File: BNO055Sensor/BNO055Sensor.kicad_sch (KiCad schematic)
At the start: 3 parts, among them J1 addon_conn

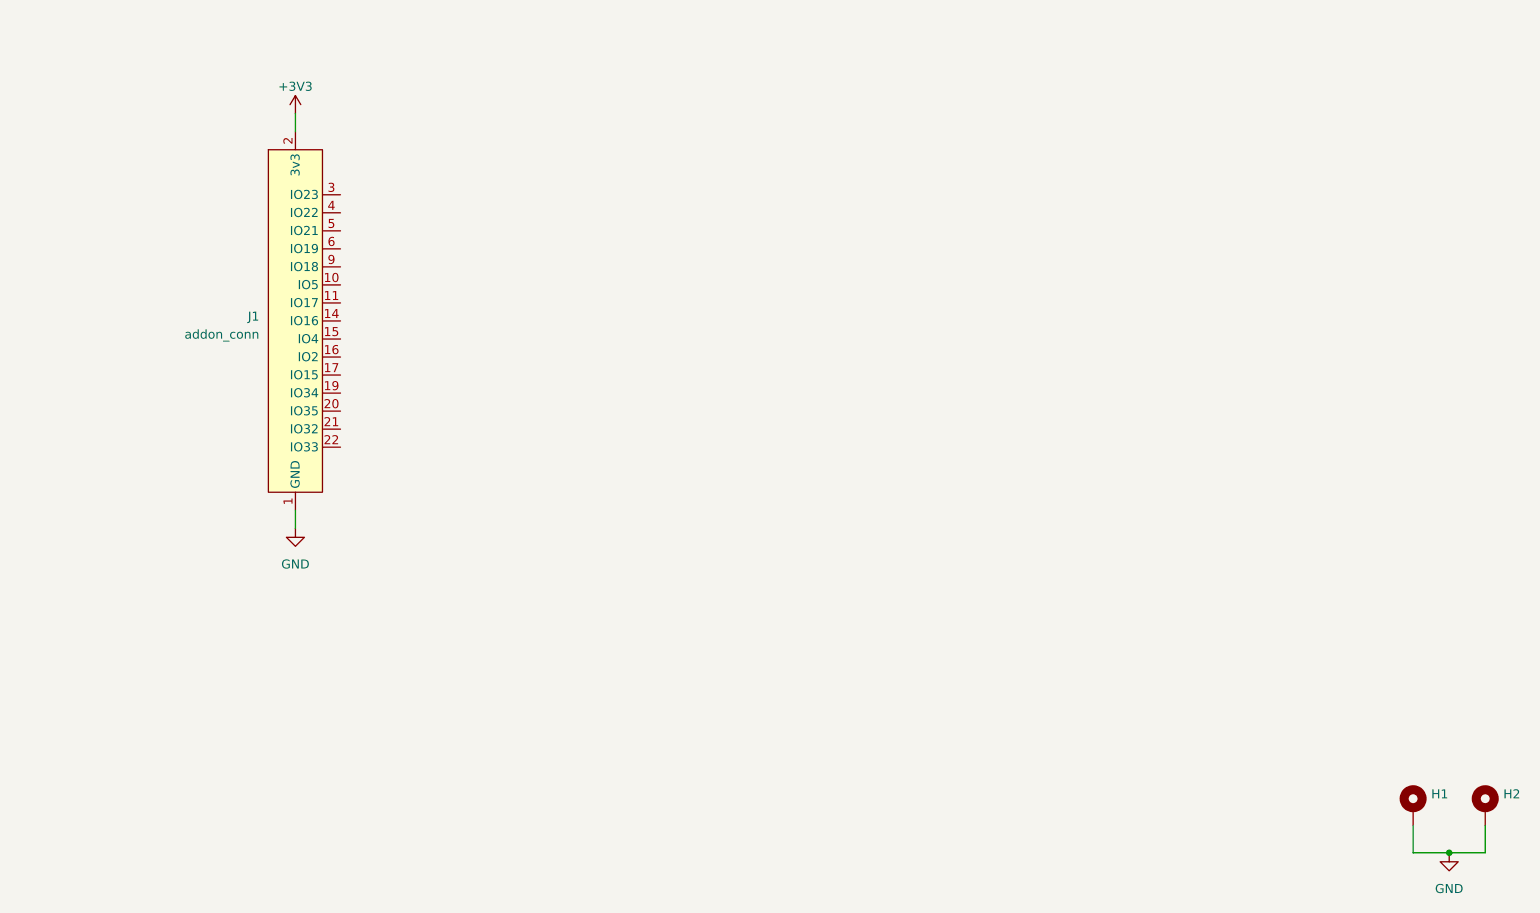
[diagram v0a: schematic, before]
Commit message: Adds BNO055 sensor to schematics
The unused pins are disconnected for now. If we have pins left after
adding other components, we can connect them.

3v3 is connected to the board through a jumper that's normally closed to
Vin since that should be the pin used. In the prototype, 3vo was used
and worked. After we confirm the PCB works with 3v3 connected to Vin as
expected, we can remove this jumper.
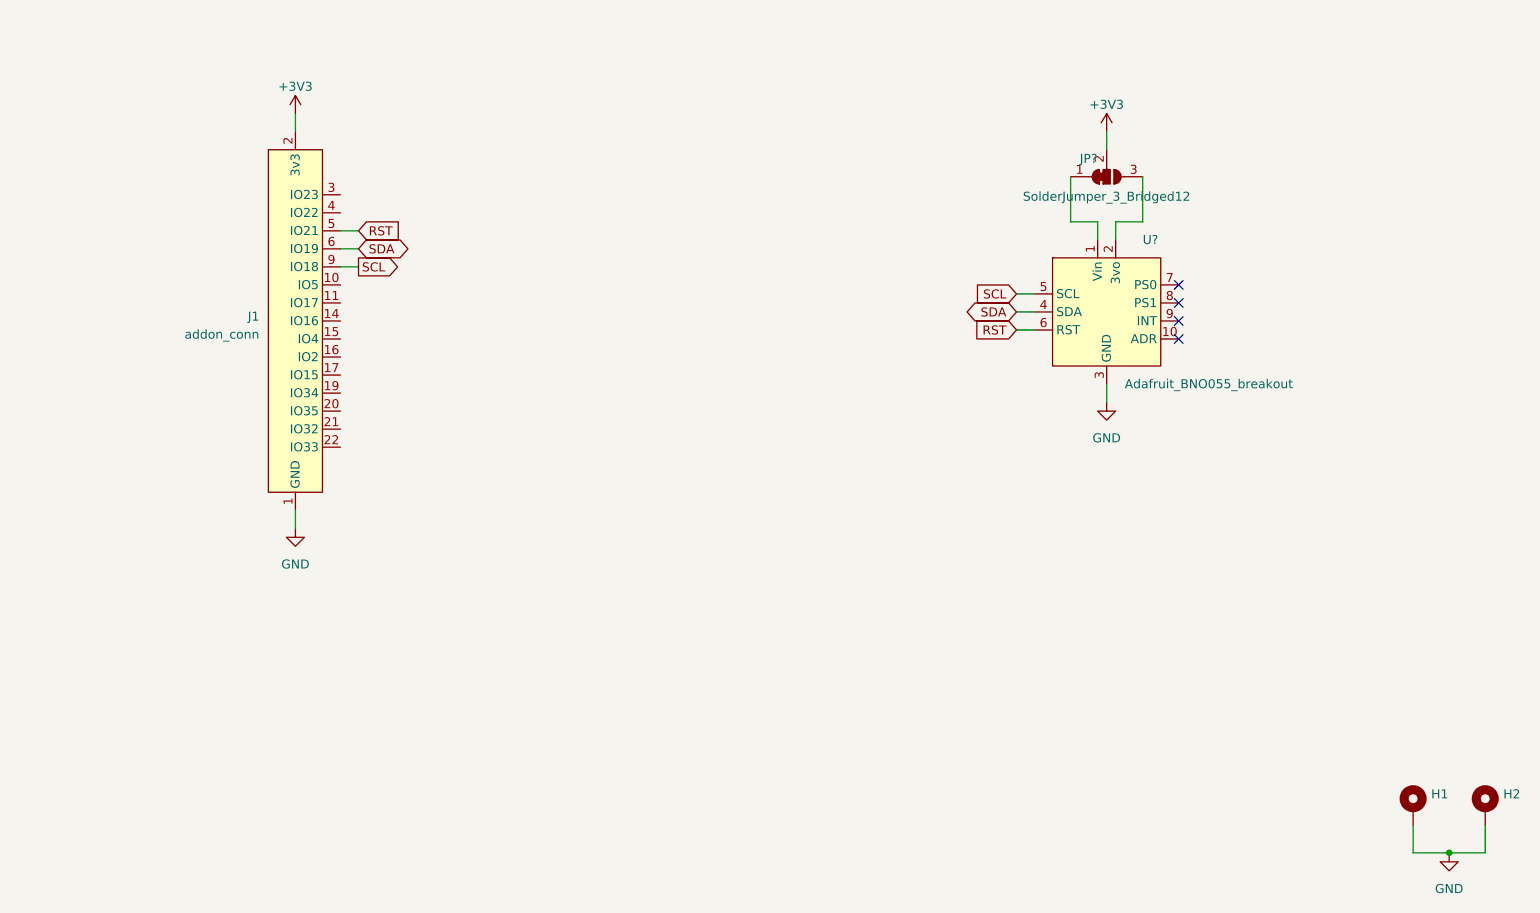
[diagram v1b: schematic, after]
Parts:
- added JP?: SolderJumper_3_Bridged12, symbol Jumper:SolderJumper_3_Bridged12
- added U?: Adafruit_BNO055_breakout, GameOver:Adafruit_BNO055_breakout, symbol GameOver:Adafruit_BNO055_breakout
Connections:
- net +3V3: now also JP?.2 (C)
- net GND: now also U?.3 (GND)
- net RST: now reaches J1.5 (IO21)
- net RST: now also U?.6 (RST)
- net SDA: now reaches J1.6 (IO19)
- net SDA: now also U?.4 (SDA)
- net SCL: now reaches J1.9 (IO18)
- net SCL: now also U?.5 (SCL)
- new net: JP?.1 (A), U?.1 (Vin)
- new net: JP?.3 (B), U?.2 (3vo)
- no-connect marks 0 -> 4
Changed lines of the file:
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@@
   (junction (at 271.78 148.59) (diameter 0) (color 0 0 0 0)
   )
+  (no_connect (at 233.68 68.58))
+  (no_connect (at 233.68 71.12))
+  (no_connect (at 233.68 73.66))
+  (no_connect (at 233.68 76.2))
   (wire (pts (xy 109.22 44.45) (xy 109.22 46.99))
     (stroke (width 0) (type default))
   )
+  (wire (pts (xy 115.57 63.5) (xy 118.11 63.5))
+    (stroke (width 0) (type default))
+  )
   (wire (pts (xy 276.86 148.59) (xy 276.86 144.78))
     (stroke (width 0) (type default))
   )
+  (wire (pts (xy 218.44 53.34) (xy 218.44 59.69))
+    (stroke (width 0) (type default))
+  )
+  (wire (pts (xy 224.79 59.69) (xy 228.6 59.69))
+    (stroke (width 0) (type default))
+  )
+  (wire (pts (xy 223.52 82.55) (xy 223.52 85.09))
+    (stroke (width 0) (type default))
+  )
+  (wire (pts (xy 115.57 60.96) (xy 118.11 60.96))
+    (stroke (width 0) (type default))
+  )
+  (wire (pts (xy 210.82 74.93) (xy 213.36 74.93))
+    (stroke (width 0) (type default))
+  )
+  (wire (pts (xy 115.57 66.04) (xy 118.11 66.04))
+    (stroke (width 0) (type default))
+  )
   (wire (pts (xy 266.7 148.59) (xy 271.78 148.59))
     (stroke (width 0) (type default))
@@
     (stroke (width 0) (type default))
   )
+  (wire (pts (xy 222.25 59.69) (xy 222.25 62.23))
+    (stroke (width 0) (type default))
+  )
+  (wire (pts (xy 210.82 69.85) (xy 213.36 69.85))
+    (stroke (width 0) (type default))
+  )
   (wire (pts (xy 271.78 148.59) (xy 276.86 148.59))
     (stroke (width 0) (type default))
@@
     (stroke (width 0) (type default))
   )
+  (wire (pts (xy 224.79 62.23) (xy 224.79 59.69))
+    (stroke (width 0) (type default))
+  )
+  (wire (pts (xy 218.44 59.69) (xy 222.25 59.69))
+    (stroke (width 0) (type default))
+  )
+  (wire (pts (xy 223.52 46.99) (xy 223.52 49.53))
+    (stroke (width 0) (type default))
+  )
+  (wire (pts (xy 228.6 59.69) (xy 228.6 53.34))
+    (stroke (width 0) (type default))
+  )
+  (wire (pts (xy 210.82 72.39) (xy 213.36 72.39))
+    (stroke (width 0) (type default))
+  )
+  (global_label "SDA" (shape bidirectional) (at 118.11 63.5 0) (fields_autoplaced)
+    (effects (font (size 1.27 1.27)) (justify left))
+    (property "Intersheetrefs" "${INTERSHEET_REFS}" (id 0) (at 125.5364 63.5 0)
+      (effects (font (size 1.27 1.27)) (justify left) hide)
+    )
+  )
+  (global_label "SDA" (shape bidirectional) (at 210.82 72.39 180) (fields_autoplaced)
+    (effects (font (size 1.27 1.27)) (justify right))
+    (property "Intersheetrefs" "${INTERSHEET_REFS}" (id 0) (at 203.3936 72.39 0)
+      (effects (font (size 1.27 1.27)) (justify right) hide)
+    )
+  )
+  (global_label "RST" (shape input) (at 118.11 60.96 0) (fields_autoplaced)
+    (effects (font (size 1.27 1.27)) (justify left))
+    (property "Intersheetrefs" "${INTERSHEET_REFS}" (id 0) (at 124.3041 60.96 0)
+      (effects (font (size 1.27 1.27)) (justify left) hide)
+    )
+  )
+  (global_label "RST" (shape input) (at 210.82 74.93 180) (fields_autoplaced)
+    (effects (font (size 1.27 1.27)) (justify right))
+    (property "Intersheetrefs" "${INTERSHEET_REFS}" (id 0) (at 204.6259 74.93 0)
+      (effects (font (size 1.27 1.27)) (justify right) hide)
+    )
+  )
+  (global_label "SCL" (shape output) (at 118.11 66.04 0) (fields_autoplaced)
+    (effects (font (size 1.27 1.27)) (justify left))
+    (property "Intersheetrefs" "${INTERSHEET_REFS}" (id 0) (at 124.3646 66.04 0)
+      (effects (font (size 1.27 1.27)) (justify left) hide)
+    )
+  )
+  (global_label "SCL" (shape input) (at 210.82 69.85 180) (fields_autoplaced)
+    (effects (font (size 1.27 1.27)) (justify right))
+    (property "Intersheetrefs" "${INTERSHEET_REFS}" (id 0) (at 204.5654 69.85 0)
+      (effects (font (size 1.27 1.27)) (justify right) hide)
+    )
+  )
   (symbol (lib_id "power:GND") (at 109.22 102.87 0) (unit 1)
     (in_bom yes) (on_board yes) (fields_autoplaced)
@@
     (pin "1")
   )
+  (symbol (lib_id "power:GND") (at 223.52 85.09 0) (unit 1)
+    (in_bom yes) (on_board yes) (fields_autoplaced)
+    (property "Reference" "#PWR?" (id 0) (at 223.52 91.44 0)
+      (effects (font (size 1.27 1.27)) hide)
+    )
+    (property "Value" "GND" (id 1) (at 223.52 90.17 0)
+      (effects (font (size 1.27 1.27)))
+    )
+    (property "Footprint" "" (id 2) (at 223.52 85.09 0)
+      (effects (font (size 1.27 1.27)) hide)
+    )
+    (property "Datasheet" "" (id 3) (at 223.52 85.09 0)
+      (effects (font (size 1.27 1.27)) hide)
+    )
+    (pin "1")
+  )
   (symbol (lib_id "Mechanical:MountingHole_Pad") (at 266.7 142.24 0) (unit 1)
     (in_bom yes) (on_board yes) (fields_autoplaced)
@@
     (pin "1")
   )
+  (symbol (lib_id "power:+3V3") (at 223.52 46.99 0) (unit 1)
+    (in_bom yes) (on_board yes) (fields_autoplaced)
+    (property "Reference" "#PWR?" (id 0) (at 223.52 50.8 0)
+      (effects (font (size 1.27 1.27)) hide)
+    )
+    (property "Value" "+3V3" (id 1) (at 223.52 43.18 0)
+      (effects (font (size 1.27 1.27)))
+    )
+    (property "Footprint" "" (id 2) (at 223.52 46.99 0)
+      (effects (font (size 1.27 1.27)) hide)
+    )
+    (property "Datasheet" "" (id 3) (at 223.52 46.99 0)
+      (effects (font (size 1.27 1.27)) hide)
+    )
+    (pin "1")
+  )
   (symbol (lib_id "power:GND") (at 271.78 148.59 0) (unit 1)
     (in_bom yes) (on_board yes) (fields_autoplaced)
@@
     )
     (pin "1")
+  )
+  (symbol (lib_id "GameOver:Adafruit_BNO055_breakout") (at 223.52 72.39 0) (unit 1)
+    (in_bom yes) (on_board yes)
+    (property "Reference" "U?" (id 0) (at 228.6 62.23 0)
+      (effects (font (size 1.27 1.27)) (justify left))
+    )
+    (property "Value" "Adafruit_BNO055_breakout" (id 1) (at 226.06 82.55 0)
+      (effects (font (size 1.27 1.27)) (justify left))
+    )
+    (property "Footprint" "GameOver:Adafruit_BNO055_breakout" (id 2) (at 223.52 72.39 0)
+      (effects (font (size 1.27 1.27)) hide)
+    )
+    (property "Datasheet" "https://learn.adafruit.com/adafruit-bno055-absolute-orientation-sensor/pinouts" (id 3) (at 223.52 72.39 0)
+      (effects (font (size 1.27 1.27)) hide)
+    )
+    (pin "10")
+    (pin "2")
+    (pin "4")
+    (pin "5")
+    (pin "6")
+    (pin "7")
+    (pin "8")
+    (pin "9")
+    (pin "1")
+    (pin "3")
   )
   (symbol (lib_id "GameOver:addon_conn") (at 109.22 73.66 0) (unit 1)
@@
     (pin "9")
   )
+  (symbol (lib_id "Jumper:SolderJumper_3_Bridged12") (at 223.52 53.34 0) (mirror x) (unit 1)
+    (in_bom yes) (on_board yes)
+    (property "Reference" "JP?" (id 0) (at 220.98 50.8 0)
+      (effects (font (size 1.27 1.27)))
+    )
+    (property "Value" "SolderJumper_3_Bridged12" (id 1) (at 223.52 56.134 0)
+      (effects (font (size 1.27 1.27)))
+    )
+    (property "Footprint" "" (id 2) (at 223.52 53.34 0)
+      (effects (font (size 1.27 1.27)) hide)
+    )
+    (property "Datasheet" "~" (id 3) (at 223.52 53.34 0)
+      (effects (font (size 1.27 1.27)) hide)
+    )
+    (pin "1")
+    (pin "2")
+    (pin "3")
+  )
   (symbol (lib_id "power:+3V3") (at 109.22 44.45 0) (unit 1)
     (in_bom yes) (on_board yes) (fields_autoplaced)
@@
       (reference "#PWR0102") (unit 1) (value "+3V3") (footprint "")
     )
+    (path "/451b7b0c-2389-42d4-aee4-1047fc4e3956"
+      (reference "#PWR?") (unit 1) (value "GND") (footprint "")
+    )
+    (path "/753b6a30-0b1f-4a06-8b11-d7071636d2b9"
+      (reference "#PWR?") (unit 1) (value "+3V3") (footprint "")
+    )
     (path "/72b8070d-6360-4ae2-9e52-c57614a73147"
       (reference "H1") (unit 1) (value "~") (footprint "MountingHole:MountingHole_2.2mm_M2_Pad_Via")
@@
       (reference "J1") (unit 1) (value "addon_conn") (footprint "GameOver:TXGA_FFC05036-24SBD113W5M_1x24_P0.50mm_Horizontal")
     )
-  )
+    (path "/cfc8d50c-9659-46eb-a01a-0c07c13d5803"
+      (reference "JP?") (unit 1) (value "SolderJumper_3_Bridged12") (footprint "")
+    )
+    (path "/a9369305-45f6-4583-af09-8897bb64b91f"
+      (reference "U?") (unit 1) (value "Adafruit_BNO055_breakout") (footprint "GameOver:Adafruit_BNO055_breakout")
+    )
+  )

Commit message: Adds RGB led to sensor board
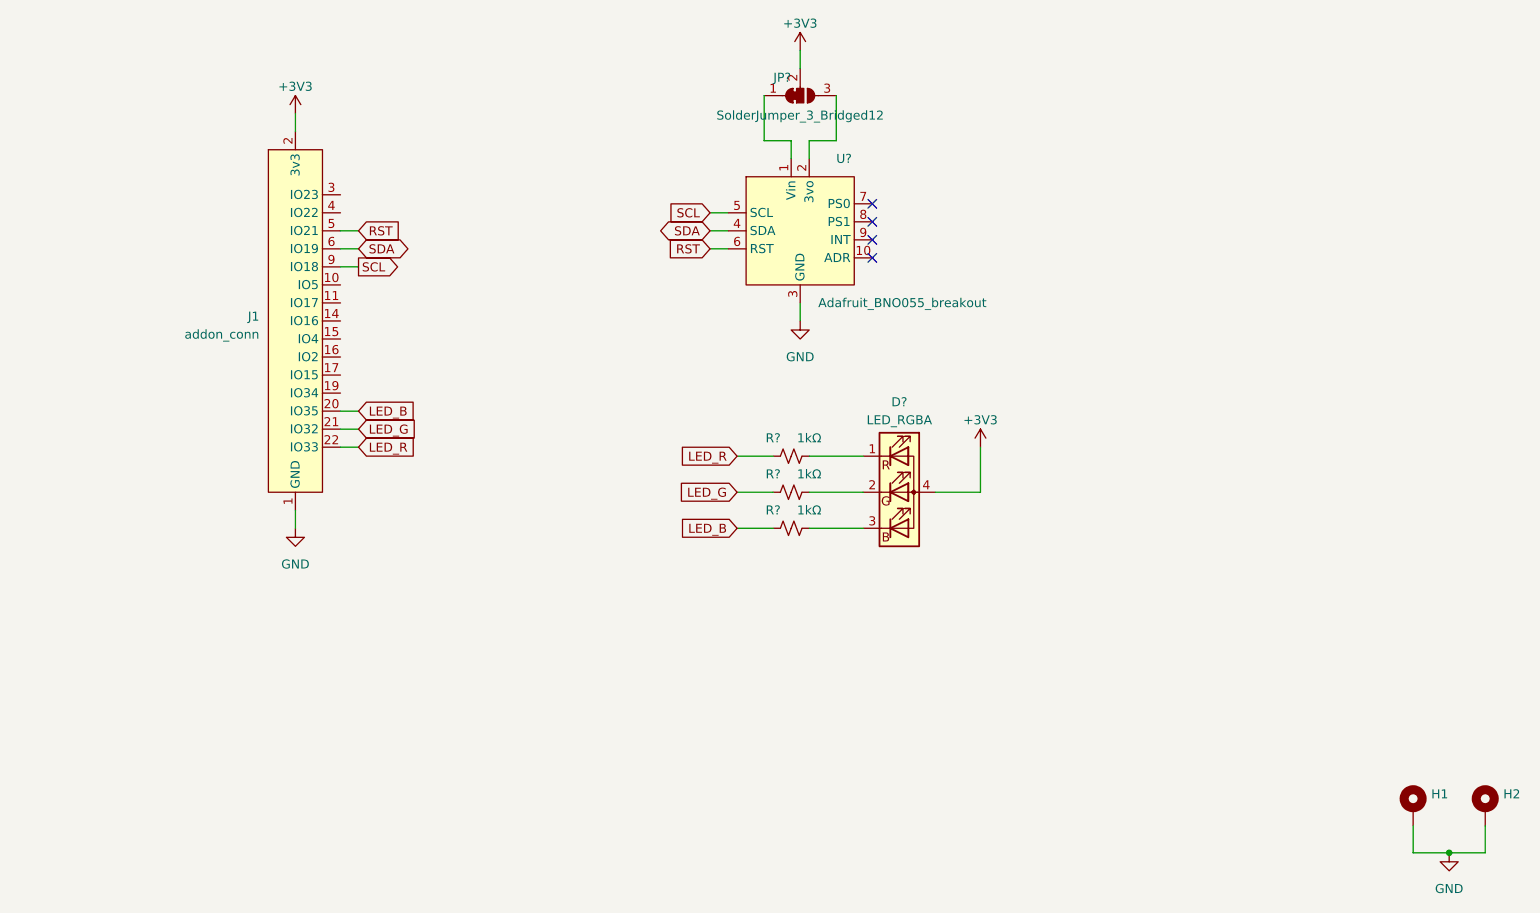
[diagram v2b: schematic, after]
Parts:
- added D?: LED_RGBA, symbol Device:LED_RGBA
- added R? (x3): 1kΩ, symbol Device:R_Small_US
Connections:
- net +3V3: now also D?.4 (A)
- net LED_B: now reaches J1.20 (IO35)
- net LED_B: now also R?.1
- net LED_G: now reaches J1.21 (IO32)
- net LED_G: now also R?.1
- net LED_R: now reaches J1.22 (IO33)
- net LED_R: now also R?.1
- new net: D?.3 (BK), R?.2
- new net: D?.2 (GK), R?.2
- new net: D?.1 (RK), R?.2
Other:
- moved on the sheet: JP?, U?

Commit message: Connects remaining pins of the BNO055 breakout board
We don't actually use them, but we had some pins left on the connector,
so we might as well connect them.
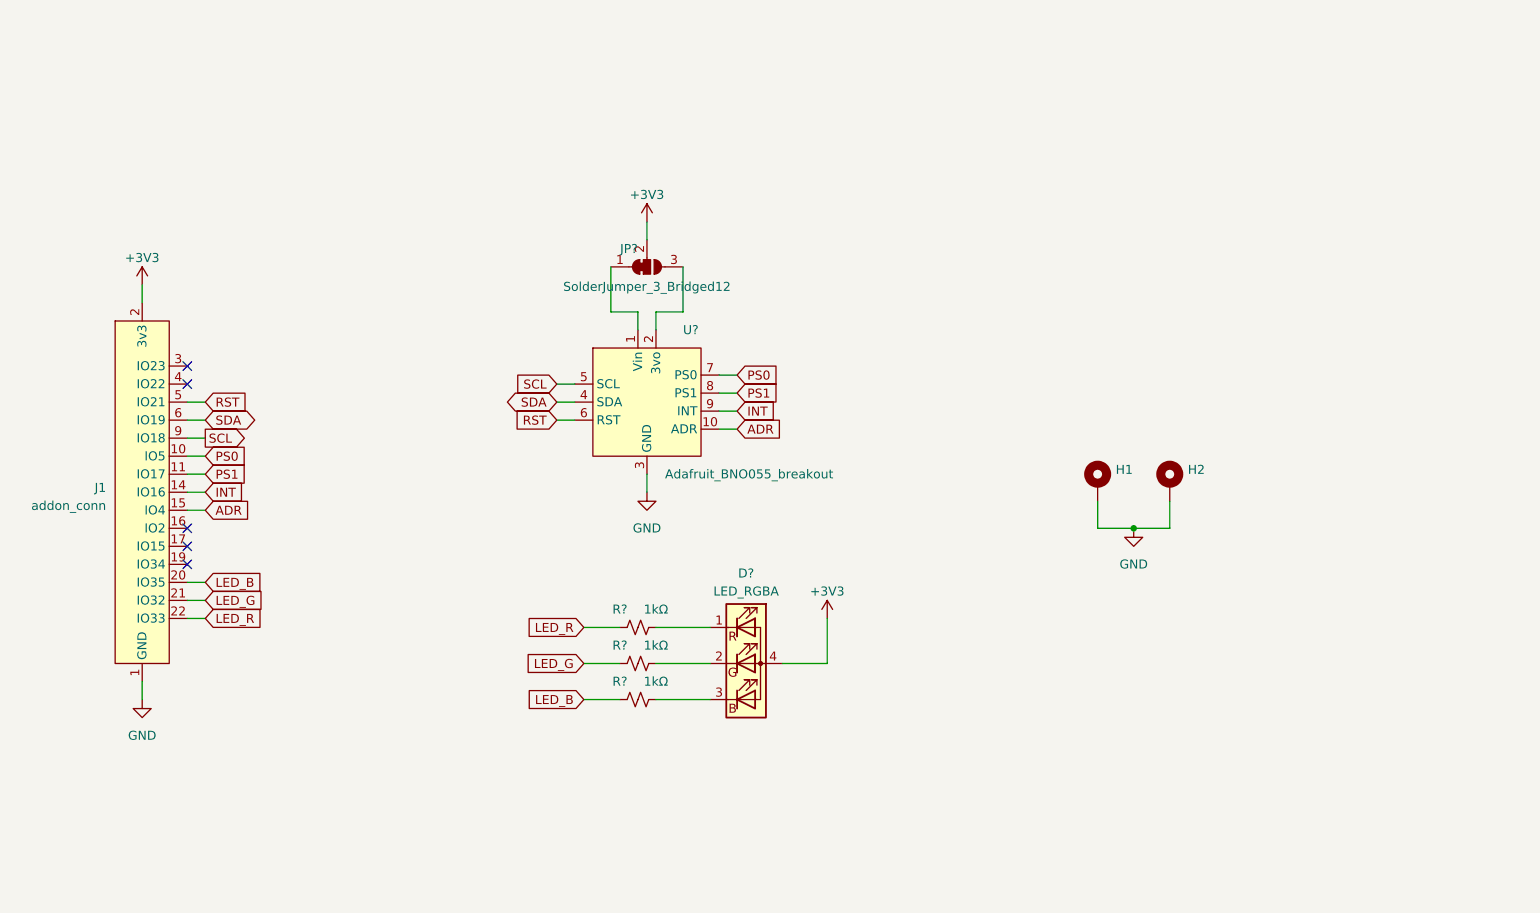
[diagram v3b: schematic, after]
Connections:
- net ADR: now reaches U?.10 (ADR)
- net ADR: now also J1.15 (IO4)
- net PS0: now reaches U?.7 (PS0)
- net PS0: now also J1.10 (IO5)
- net PS1: now reaches U?.8 (PS1)
- net PS1: now also J1.11 (IO17)
- net INT: now reaches U?.9 (INT)
- net INT: now also J1.14 (IO16)
- no-connect marks 4 -> 5
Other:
- moved on the sheet: D?, H1, H2, J1, JP?, R?, U?
